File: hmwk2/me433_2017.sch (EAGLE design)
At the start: 0 parts

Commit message: made changed to pikit3 in lbr and editting schem
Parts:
- added C1, C2, C3: (no value), resistor:C-US025-025X050
- added J1, J2: (no value), me433_2017:CONN_08
- added LED1, LED2: (no value), led:LED3MM
- added R1, R2, R3, R4: (no value), resistor:R-US_0207/10
- added U$1: PIC32MX250F128B, me433_2017:PIC32MX250F128B
- added U$2: SLIDE, me433_2017:SLIDE
- added U$3: MCP1702, me433_2017:MCP1702
- added U$4, U$5: PB, me433_2017:PB
- added U$6: PICKIT3, me433_2017:PICKIT3
- added U$7: OSC, me433_2017:OSC

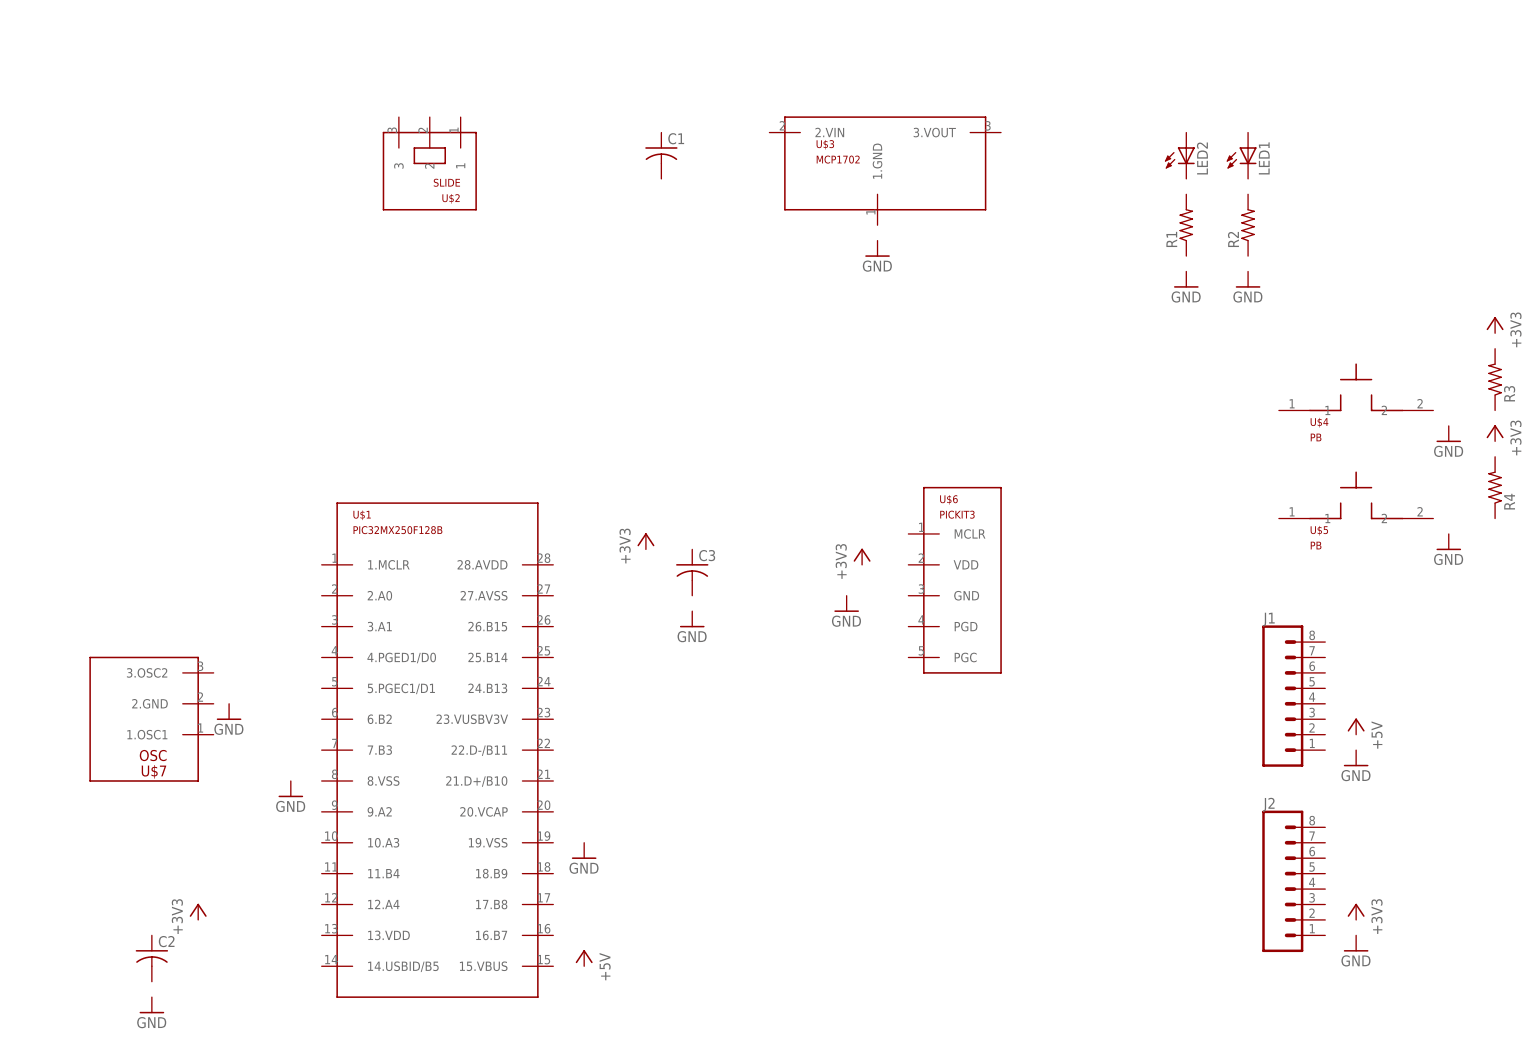
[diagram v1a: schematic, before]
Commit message: made changes to USB in lbr and continued schematic
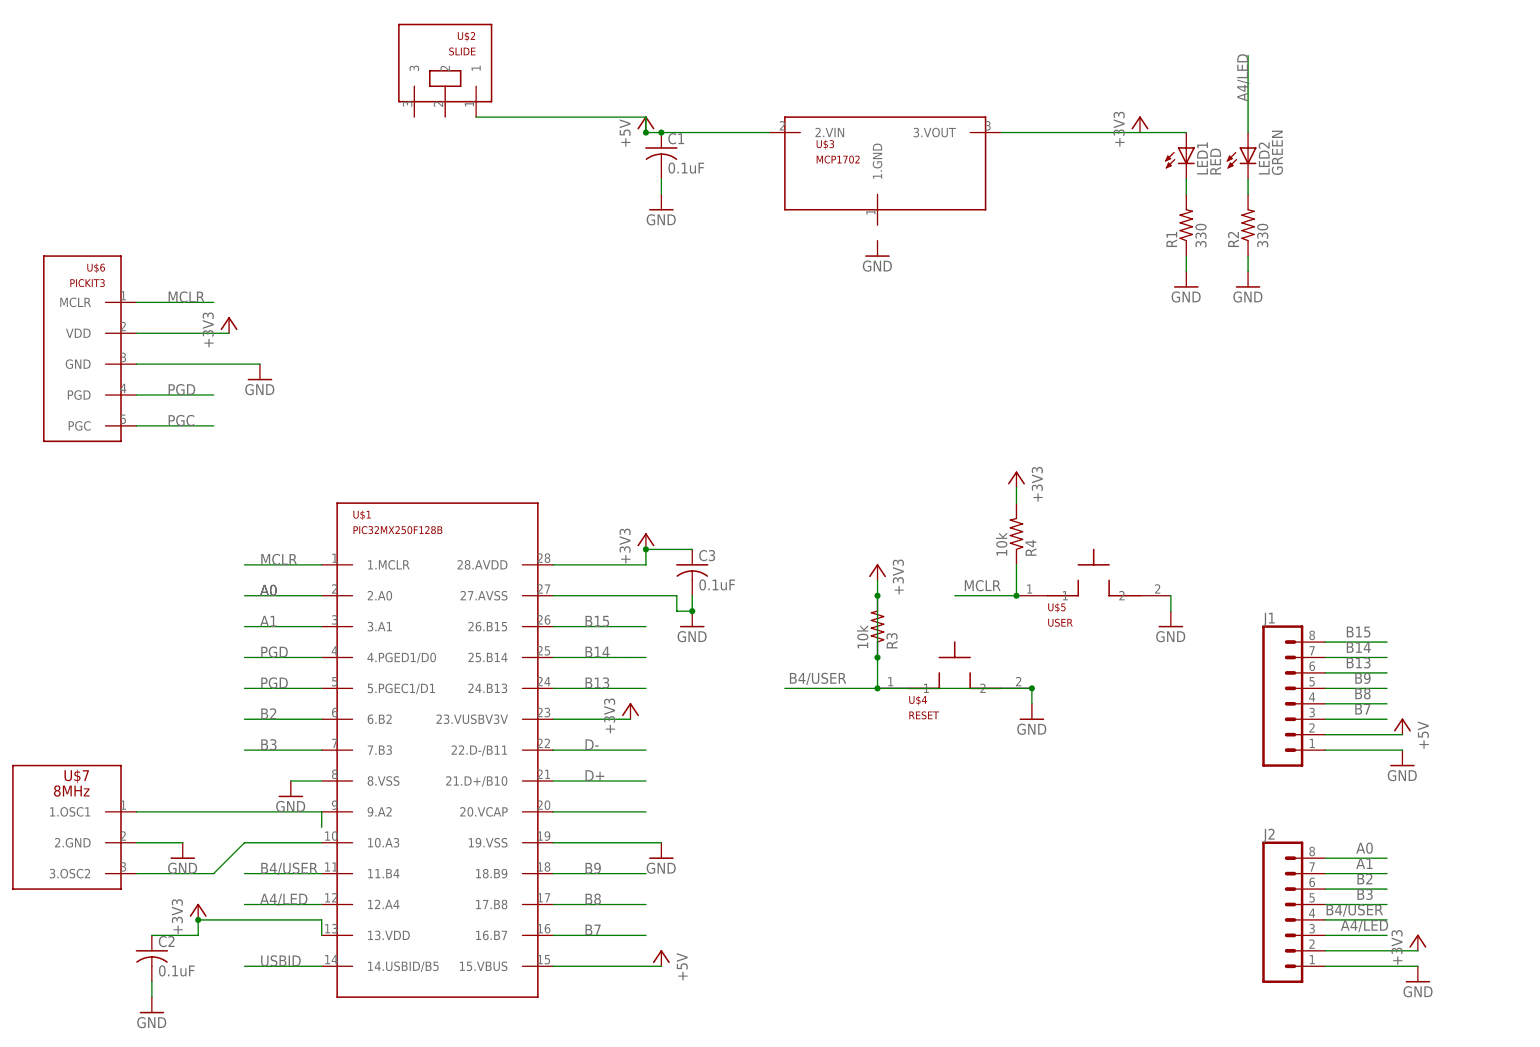
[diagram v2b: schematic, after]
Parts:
- C1, C2, C3: value (none) -> 0.1uF
- LED1: value (none) -> RED
- LED2: value (none) -> GREEN
- R1, R2: value (none) -> 330
- R3, R4: value (none) -> 10k
- U$4: value PB -> RESET
- U$5: value PB -> USER
- U$7: value OSC -> 8MHz
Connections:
- new net +3V3: C2.1, C3.1, J2.2, R4.2, U$1.13.VDD, U$1.23.VUSBV3V, U$1.28.AVDD, U$6.VDD
- new net +5V: C1.1, J1.2, U$1.15.VBUS, U$2.1, U$3.2.VIN
- new net A0: J2.8, U$1.2.A0
- new net A1: J2.7, U$1.3.A1
- new net A4/LED: J2.3, LED2.A, U$1.12.A4
- new net B13: J1.6, U$1.24.B13
- new net B14: J1.7, U$1.25.B14
- new net B15: J1.8, U$1.26.B15
- new net B2: J2.6, U$1.6.B2
- new net B3: J2.5, U$1.7.B3
- new net B4/USER: J2.4, R3.1, R3.2, U$1.11.B4, U$4.1, U$4.2
- new net B7: J1.3, U$1.16.B7
- new net B8: J1.4, U$1.17.B8
- new net B9: J1.5, U$1.18.B9
- new net D+: U$1.21.D+/B10
- new net D-: U$1.22.D-/B11
- new net GND: C1.2, C2.2, C3.2, J1.1, J2.1, R1.1, R2.1, U$1.19.VSS, U$1.27.AVSS, U$1.8.VSS, U$5.2, U$6.GND, U$7.2.GND
- new net MCLR: R4.1, U$1.1.MCLR, U$5.1, U$6.MCLR
- new net N$1: LED1.A, U$3.3.VOUT
- new net N$17: U$1.20.VCAP
- new net N$2: LED1.C, R1.2
- new net N$3: U$7.1.OSC1
- new net N$33: LED2.C, R2.2
- new net N$4: U$1.10.A3, U$7.3.OSC2
- new net N$9: U$1.5.PGEC1/D1
- new net PGC: U$6.PGC
- new net PGD: U$1.4.PGED1/D0, U$6.PGD
- new net USBID: U$1.14.USBID/B5
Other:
- moved on the sheet: J2, LED1, LED2, R3, R4, U$2, U$4, U$5, U$6, U$7

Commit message: added usb and polar capacitors to schematics
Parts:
- added C4, C6: 10uF, rcl:CPOL-USB45181B
- added C7: 0.1uF, rcl:C-US025-025X050
- added J3: USB, me433_2017:USB
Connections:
- removed net N$1: LED1.A, U$3.3.VOUT
- new net VBUS: J3.VBUS, U$2.2
- net +3V3: now also C6.+, C7.1, LED1.A, U$3.3.VOUT
- net +5V: now also U$2.3; no longer U$2.1
- net D+: now also J3.D+
- net D-: now also J3.D-
- net GND: now also C4.-, J3.GND
- net N$17: now also C4.+
- net USBID: now also J3.ID
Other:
- moved on the sheet: U$2
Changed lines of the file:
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@@
 <part name="+3V9" library="supply1" deviceset="+3V3" device=""/>
 <part name="GND15" library="supply1" deviceset="GND" device=""/>
+<part name="C4" library="rcl" deviceset="CPOL-US" device="B45181B" value="10uF"/>
+<part name="C6" library="rcl" deviceset="CPOL-US" device="B45181B" value="10uF"/>
+<part name="C7" library="rcl" deviceset="C-US" device="025-025X050" value="0.1uF"/>
+<part name="GND4" library="supply1" deviceset="GND" device=""/>
+<part name="J3" library="me433_2017" deviceset="USB" device=""/>
+<part name="GND16" library="supply1" deviceset="GND" device=""/>
 </parts>
 <sheets>
@@
 <instances>
 <instance part="U$1" gate="G$1" x="60.96" y="27.94"/>
-<instance part="U$2" gate="G$1" x="63.5" y="134.62" rot="MR0"/>
+<instance part="U$2" gate="G$1" x="68.58" y="134.62"/>
 <instance part="U$3" gate="G$1" x="134.62" y="127"/>
 <instance part="LED2" gate="G$1" x="195.58" y="124.46"/>
@@
 <instance part="+3V9" gate="G$1" x="27.94" y="96.52"/>
 <instance part="GND15" gate="1" x="33.02" y="86.36"/>
+<instance part="C4" gate="G$1" x="106.68" y="12.7"/>
+<instance part="C6" gate="G$1" x="167.64" y="121.92"/>
+<instance part="C7" gate="G$1" x="160.02" y="121.92"/>
+<instance part="GND4" gate="1" x="106.68" y="2.54"/>
+<instance part="J3" gate="G$1" x="10.16" y="132.08" rot="MR0"/>
+<instance part="GND16" gate="1" x="17.78" y="129.54"/>
 </instances>
 <busses>
@@
 <net name="+5V" class="0">
 <segment>
-<pinref part="U$2" gate="G$1" pin="1"/>
 <pinref part="P+3" gate="1" pin="+5V"/>
-<wire x1="68.58" y1="129.54" x2="96.52" y2="129.54" width="0.1524" layer="91"/>
-<wire x1="96.52" y1="129.54" x2="96.52" y2="127" width="0.1524" layer="91"/>
 <pinref part="C1" gate="G$1" pin="1"/>
 <wire x1="96.52" y1="127" x2="99.06" y2="127" width="0.1524" layer="91"/>
@@
 <wire x1="99.06" y1="127" x2="116.84" y2="127" width="0.1524" layer="91"/>
 <junction x="99.06" y="127"/>
+<pinref part="U$2" gate="G$1" pin="3"/>
+<wire x1="73.66" y1="129.54" x2="96.52" y2="129.54" width="0.1524" layer="91"/>
+<wire x1="96.52" y1="129.54" x2="96.52" y2="127" width="0.1524" layer="91"/>
 </segment>
 <segment>
@@
 <wire x1="208.28" y1="25.4" x2="220.98" y2="25.4" width="0.1524" layer="91"/>
 </segment>
-</net>
-<net name="N$1" class="0">
-<segment>
-<pinref part="U$3" gate="G$1" pin="3.VOUT"/>
-<pinref part="LED1" gate="G$1" pin="A"/>
-<wire x1="154.94" y1="127" x2="185.42" y2="127" width="0.1524" layer="91"/>
+<segment>
+<pinref part="C4" gate="G$1" pin="-"/>
+<pinref part="GND4" gate="1" pin="GND"/>
+<wire x1="106.68" y1="7.62" x2="106.68" y2="5.08" width="0.1524" layer="91"/>
+</segment>
+<segment>
+<pinref part="J3" gate="G$1" pin="GND"/>
+<pinref part="GND16" gate="1" pin="GND"/>
+<wire x1="12.7" y1="132.08" x2="17.78" y2="132.08" width="0.1524" layer="91"/>
 </segment>
 </net>
@@
 <wire x1="157.48" y1="68.58" x2="157.48" y2="66.04" width="0.1524" layer="91"/>
 </segment>
+<segment>
+<pinref part="U$3" gate="G$1" pin="3.VOUT"/>
+<pinref part="C7" gate="G$1" pin="1"/>
+<wire x1="154.94" y1="127" x2="160.02" y2="127" width="0.1524" layer="91"/>
+<wire x1="160.02" y1="127" x2="160.02" y2="124.46" width="0.1524" layer="91"/>
+<pinref part="C6" gate="G$1" pin="+"/>
+<wire x1="160.02" y1="124.46" x2="167.64" y2="124.46" width="0.1524" layer="91"/>
+<junction x="160.02" y="124.46"/>
+<pinref part="+3V7" gate="G$1" pin="+3V3"/>
+<wire x1="167.64" y1="124.46" x2="177.8" y2="124.46" width="0.1524" layer="91"/>
+<wire x1="177.8" y1="124.46" x2="177.8" y2="127" width="0.1524" layer="91"/>
+<junction x="167.64" y="124.46"/>
+<wire x1="177.8" y1="124.46" x2="180.34" y2="124.46" width="0.1524" layer="91"/>
+<junction x="177.8" y="124.46"/>
+<wire x1="180.34" y1="124.46" x2="180.34" y2="129.54" width="0.1524" layer="91"/>
+<wire x1="180.34" y1="129.54" x2="185.42" y2="129.54" width="0.1524" layer="91"/>
+<pinref part="LED1" gate="G$1" pin="A"/>
+<wire x1="185.42" y1="129.54" x2="185.42" y2="127" width="0.1524" layer="91"/>
+</segment>
 </net>
 <net name="N$3" class="0">
@@
 <wire x1="81.28" y1="20.32" x2="96.52" y2="20.32" width="0.1524" layer="91"/>
 <label x="86.36" y="20.32" size="1.778" layer="95"/>
+</segment>
+<segment>
+<pinref part="J3" gate="G$1" pin="D+"/>
+<wire x1="12.7" y1="139.7" x2="22.86" y2="139.7" width="0.1524" layer="91"/>
+<label x="15.24" y="139.7" size="1.778" layer="95"/>
 </segment>
 </net>
@@
 <label x="33.02" y="-10.16" size="1.778" layer="95"/>
 </segment>
+<segment>
+<pinref part="J3" gate="G$1" pin="ID"/>
+<wire x1="12.7" y1="142.24" x2="22.86" y2="142.24" width="0.1524" layer="91"/>
+<label x="15.24" y="142.24" size="1.778" layer="95"/>
+</segment>
 </net>
 <net name="D-" class="0">
@@
 <wire x1="81.28" y1="25.4" x2="96.52" y2="25.4" width="0.1524" layer="91"/>
 <label x="86.36" y="25.4" size="1.778" layer="95"/>
+</segment>
+<segment>
+<pinref part="J3" gate="G$1" pin="D-"/>
+<wire x1="12.7" y1="137.16" x2="22.86" y2="137.16" width="0.1524" layer="91"/>
+<label x="15.24" y="137.16" size="1.778" layer="95"/>
 </segment>
 </net>
@@
 <segment>
 <pinref part="U$1" gate="G$1" pin="20.VCAP"/>
-<wire x1="81.28" y1="15.24" x2="96.52" y2="15.24" width="0.1524" layer="91"/>
+<wire x1="81.28" y1="15.24" x2="106.68" y2="15.24" width="0.1524" layer="91"/>
+<pinref part="C4" gate="G$1" pin="+"/>
 </segment>
 </net>
@@
 </segment>
 </net>
+<net name="VBUS" class="0">
+<segment>
+<pinref part="J3" gate="G$1" pin="VBUS"/>
+<wire x1="12.7" y1="134.62" x2="53.34" y2="134.62" width="0.1524" layer="91"/>
+<wire x1="53.34" y1="134.62" x2="53.34" y2="124.46" width="0.1524" layer="91"/>
+<pinref part="U$2" gate="G$1" pin="2"/>
+<wire x1="53.34" y1="124.46" x2="68.58" y2="124.46" width="0.1524" layer="91"/>
+<wire x1="68.58" y1="124.46" x2="68.58" y2="129.54" width="0.1524" layer="91"/>
+<label x="17.78" y="134.62" size="1.778" layer="95"/>
+</segment>
+</net>

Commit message: made a small changed to gnd connection on regulator
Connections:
- net GND: now also U$3.1.GND
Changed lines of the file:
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@@
 <wire x1="12.7" y1="132.08" x2="17.78" y2="132.08" width="0.1524" layer="91"/>
+</segment>
+<segment>
+<pinref part="U$3" gate="G$1" pin="1.GND"/>
+<pinref part="GND5" gate="1" pin="GND"/>
+<wire x1="134.62" y1="111.76" x2="134.62" y2="109.22" width="0.1524" layer="91"/>
 </segment>
 </net>
